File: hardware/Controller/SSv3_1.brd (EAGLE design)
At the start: 127 x 100.1 mm, 197 parts, among them Q1 20.000_MHZ, Q2 200mA/50V, X1 PN61729-S, X2 SCAN_LED, X3 RJ45-6L-B, X4 C-GRID-06-74099

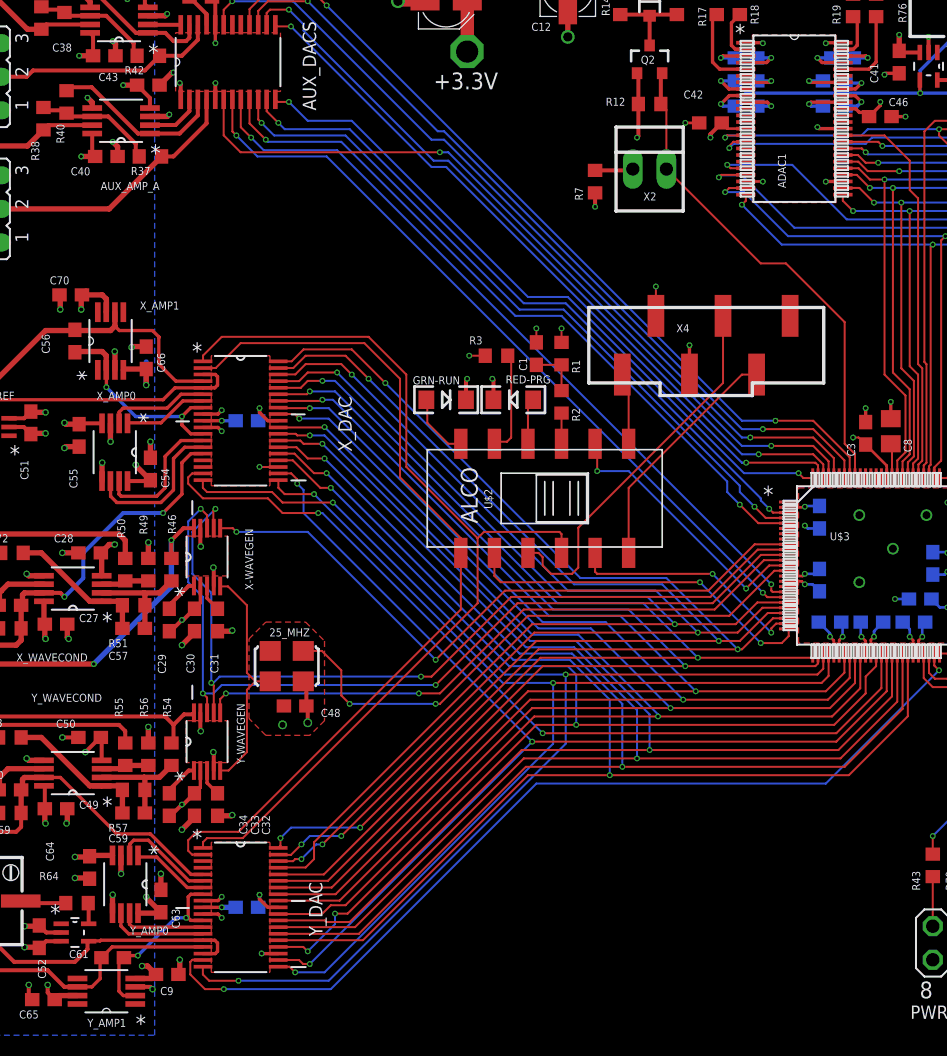
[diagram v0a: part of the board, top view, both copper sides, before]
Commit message: Cleaned up DRC warnings from switch to Eagle 9.3
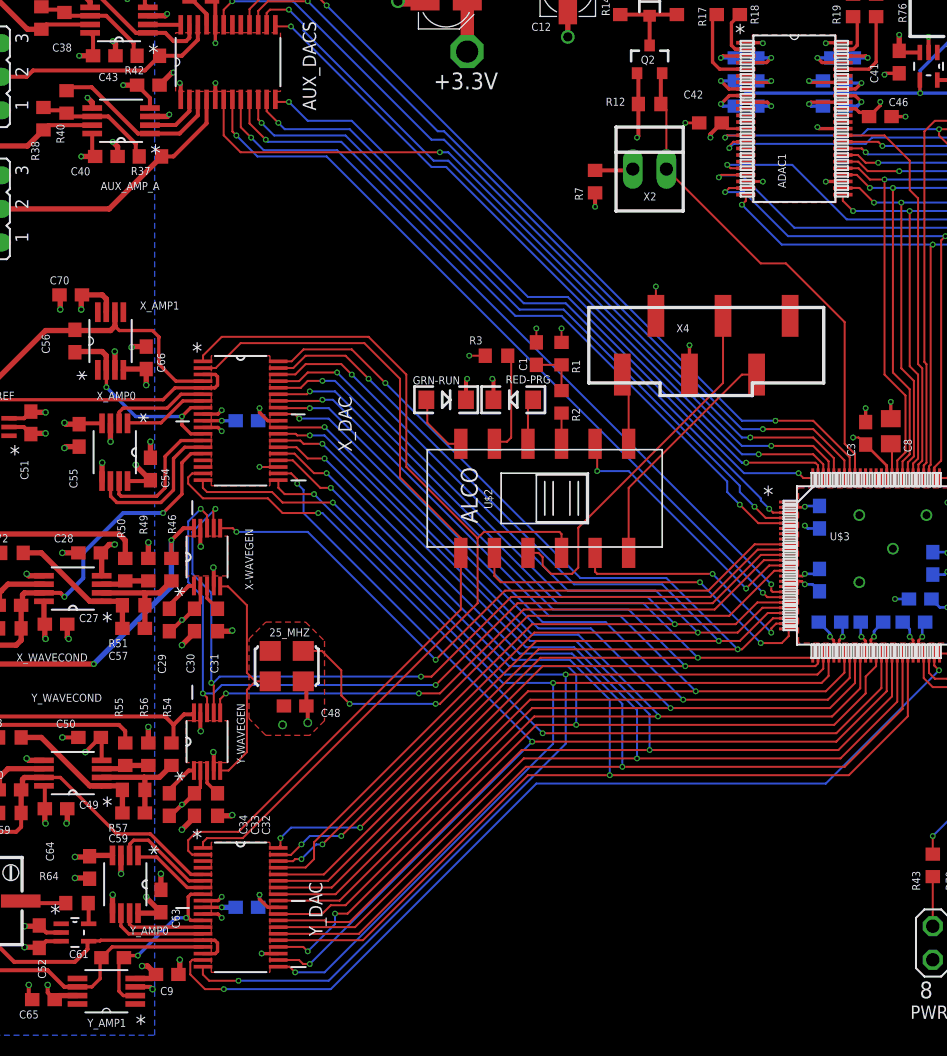
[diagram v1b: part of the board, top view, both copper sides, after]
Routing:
- net -12V: track 36.2 -> 34.1 mm
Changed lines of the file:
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@@
 <contactref element="X4" pad="2"/>
 <via x="87.15375" y="47.78375" extent="1-16" drill="0.254"/>
-<wire x1="88.05" y1="47.3075" x2="88.10625" y2="47.25125" width="0.254" layer="1"/>
 <wire x1="89.699996875" y1="44.7167" x2="89.699996875" y2="45.657503125" width="0.2032" layer="1"/>
 <wire x1="89.699996875" y1="45.657503125" x2="88.10625" y2="47.25125" width="0.2032" layer="1"/>
@@
 <wire x1="25.97875" y1="19.685" x2="25.97875" y2="21.35415" width="0.3048" layer="1"/>
 <wire x1="25.97875" y1="21.35415" x2="25.91435" y2="21.41855" width="0.3048" layer="1"/>
-<wire x1="29.0948" y1="58.88355" x2="28.79" y2="58.57875" width="0.4064" layer="1"/>
 <wire x1="23.2664" y1="49.2379" x2="24.41665" y2="49.2379" width="0.3048" layer="1"/>
 <wire x1="24.41665" y1="49.2379" x2="24.92375" y2="49.745" width="0.3048" layer="1"/>
@@
 <via x="33.655" y="51.7525" extent="1-16" drill="0.3048"/>
 <wire x1="33.655" y1="52.96625" x2="33.655" y2="51.7525" width="0.4064" layer="1"/>
-<wire x1="33.655" y1="51.7525" x2="33.655" y2="53.49875" width="0.4064" layer="16"/>
 <via x="29.05125" y="23.97125" extent="1-16" drill="0.3048"/>
 <wire x1="30.21875" y1="25.0825" x2="30.1625" y2="25.0825" width="0.3048" layer="1"/>
@@
 <wire x1="16.98625" y1="52.86375" x2="15.38625" y2="52.86375" width="0.8128" layer="1"/>
 <wire x1="15.38625" y1="52.86375" x2="15.24" y2="53.01" width="0.8128" layer="1"/>
-<wire x1="34.13125" y1="7.405" x2="34.3925" y2="7.14375" width="0.4064" layer="1"/>
 <wire x1="32.82315" y1="6.83895" x2="34.0877" y2="6.83895" width="0.4064" layer="1"/>
 <wire x1="34.0877" y1="6.83895" x2="34.3925" y2="7.14375" width="0.4064" layer="1"/>
@@
 <wire x1="110.33125" y1="73.3425" x2="109.7525" y2="73.3425" width="0.254" layer="16"/>
 <wire x1="109.7525" y1="73.3425" x2="109.27625" y2="72.86625" width="0.254" layer="16"/>
-<wire x1="86.51875" y1="74.715" x2="86.575" y2="74.77125" width="0.254" layer="16"/>
 <wire x1="110.009990625" y1="73.663759375" x2="110.33125" y2="73.3425" width="0.254" layer="1"/>
 <wire x1="109.27625" y1="74.77125" x2="108.3555" y2="73.8505" width="0.254" layer="16"/>
